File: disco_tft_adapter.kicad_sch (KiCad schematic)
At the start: 0 parts

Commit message: [schematics] addded connectors and adapter wiring
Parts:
- added J1: F31L-1A7H1-11030, aa_prj:F31L1A7H111030, symbol aa_prj:F31L-1A7H1-11030
- added J2: QTH-030-02-L-D-A, aa_prj:QTH-030-XX-Y-D-A, symbol aa_prj:QTH-030-02-L-D-A
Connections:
- new net CTP_INT: J1.25, J2.4
- new net CTP_SCL: J1.27, J2.44
- new net CTP_SDA: J1.26, J2.40
- new net DSI_CLK_N: J1.17, J2.5
- new net DSI_CLK_P: J1.16, J2.3
- new net DSI_D0_N: J1.11, J2.11
- new net DSI_D0_P: J1.10, J2.9
- new net DSI_D1_N: J1.14, J2.17
- new net DSI_D1_P: J1.13, J2.15
- new net GND: J1.12, J1.15, J1.18, J1.21, J1.24, J1.31 (MP_1), J1.32 (MP_2), J1.9, J2.1, J2.13, J2.19, J2.27, J2.29, J2.7
- new net LEDA: J1.1
- new net LEDK: J1.2, J1.3
- new net PWM: J1.8
- new net PWM_UC: J2.53
- new net RST: J1.28, J1.6, J2.57
- new net TE: J1.7, J2.49
- new net VCC: J1.29, J1.30, J1.4, J1.5, J2.36
- new net VCC_BL: J2.21, J2.23
- no-connect marks 0 -> 43
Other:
- note added: "Vcc = 3V3"
- note added: "Vcc_BL = 5V"

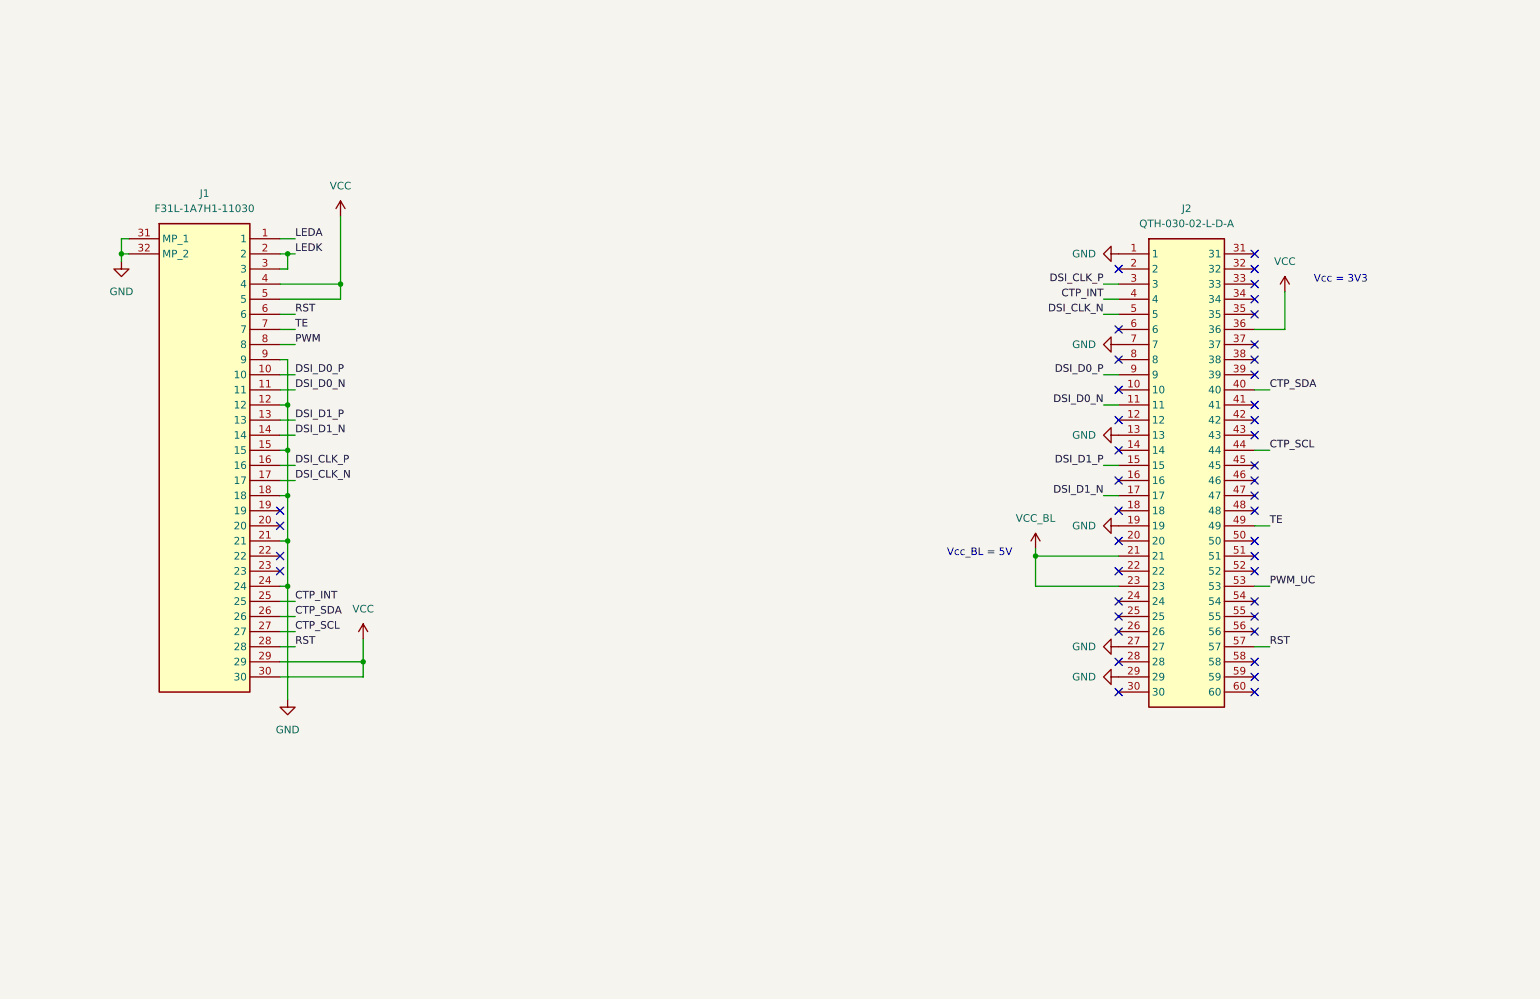
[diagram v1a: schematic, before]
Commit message: [schematics] add: buck converter for backlight control
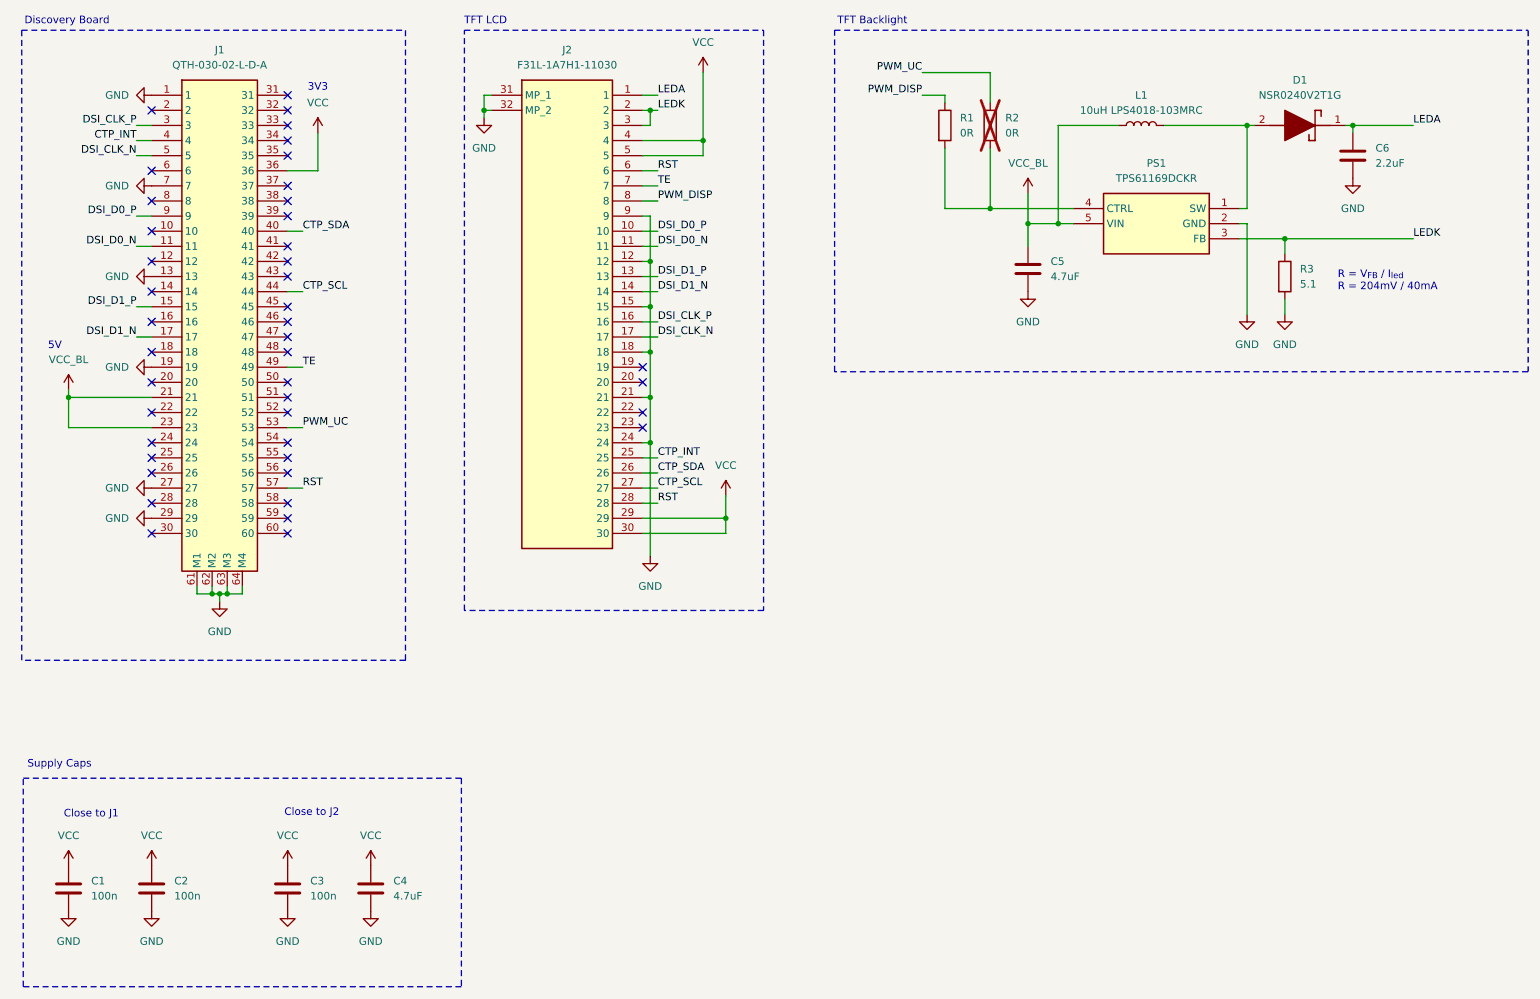
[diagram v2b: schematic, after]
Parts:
- added C1, C2, C3: 100n, Capacitor_SMD:C_0201_0603Metric_Pad0.64x0.40mm_HandSolder, symbol Device:C
- added C4, C5: 4.7uF, Capacitor_SMD:C_0805_2012Metric_Pad1.18x1.45mm_HandSolder, symbol Device:C
- added C6: 2.2uF, Capacitor_SMD:C_0805_2012Metric_Pad1.18x1.45mm_HandSolder, symbol Device:C
- added D1: NSR0240V2T1G, aa_prj:SODFL1608X70N, symbol aa_prj:NSR0240V2T1G
- added L1: 10uH LPS4018-103MRC, Inductor_SMD:L_Coilcraft_1515SQ-47N, symbol Device:L
- added PS1: TPS61169DCKR, aa_prj:SOT65P210X110-5N, symbol aa_prj:TPS61169DCKR
- added R1, R2: 0R, Resistor_SMD:R_0201_0603Metric_Pad0.64x0.40mm_HandSolder, symbol Device:R
- added R3: 5.1, Resistor_SMD:R_1206_3216Metric, symbol Device:R
- renumbered J2 to J1, J1 to J2
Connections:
- net GND: now also J1.61 (M1), J1.62 (M2), J1.63 (M3), J1.64 (M4), C1.2, C2.2, C3.2, C4.2, C5.2, C6.2, PS1.2 (GND), R3.2
- net LEDA: now also C6.1, D1.1 (K)
- net LEDK: now also PS1.3 (FB), R3.1
- net PWM_UC: now also R2.1
- net VCC: now also C1.1, C2.1, C3.1, C4.1
- net VCC_BL: now also C5.1, L1.1, PS1.5 (VIN)
- net PWM renamed PWM_DISP
- net PWM_DISP: now also R1.1
- new net: D1.2 (A), L1.2, PS1.1 (SW)
- new net: PS1.4 (CTRL), R1.2, R2.2
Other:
- note added: "3V3"
- note added: "5V"
- note added: "Close to J1"
- note added: "Close to J2"
- note added: "Discovery Board"
- note added: "R = V_{FB} / I_{led} R = 204mV / 40mA"
- note added: "Supply Caps"
- note added: "TFT Backlight"
- note added: "TFT LCD"
- note removed: "Vcc = 3V3"
- note removed: "Vcc_BL = 5V"
- moved on the sheet: J2

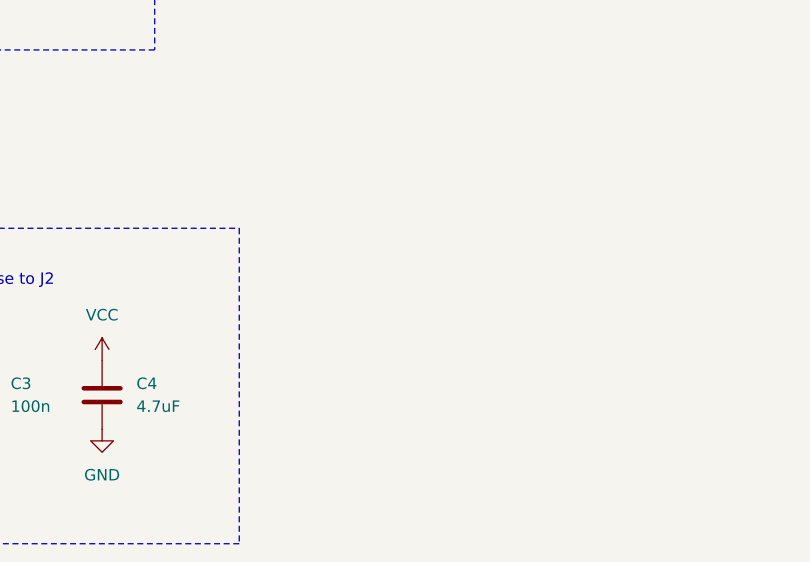
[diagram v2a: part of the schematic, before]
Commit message: [schematics] add: mounting holes
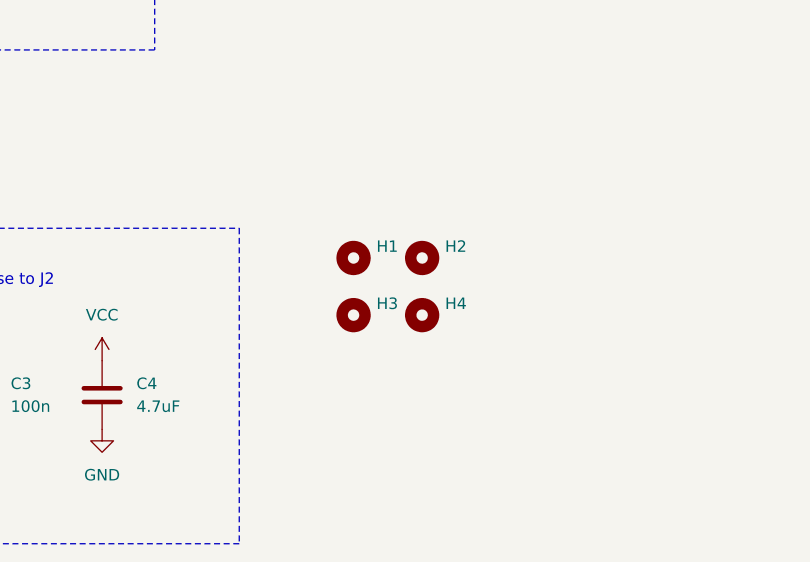
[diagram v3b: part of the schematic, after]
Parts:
- added H1, H2, H3, H4: MountingHole, MountingHole:MountingHole_4.5mm_Pad_TopBottom, symbol Mechanical:MountingHole

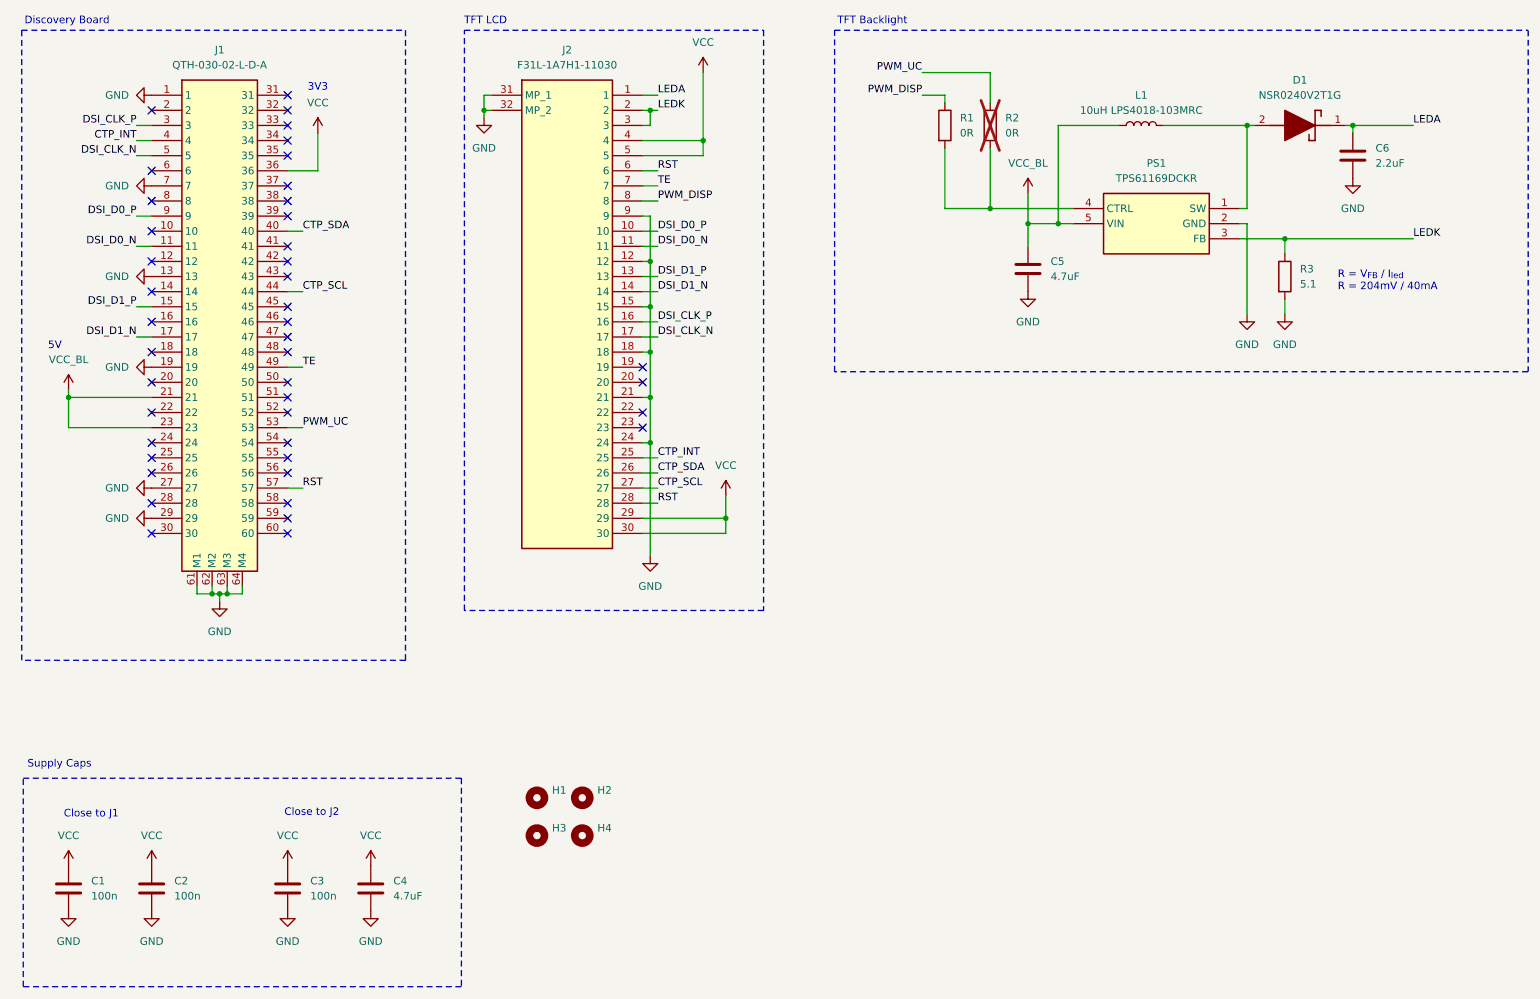
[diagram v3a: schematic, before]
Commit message: [layout] add: stitching vias, planes updated, routed buck converter for LED BL, added power labels to buck converter in schematics
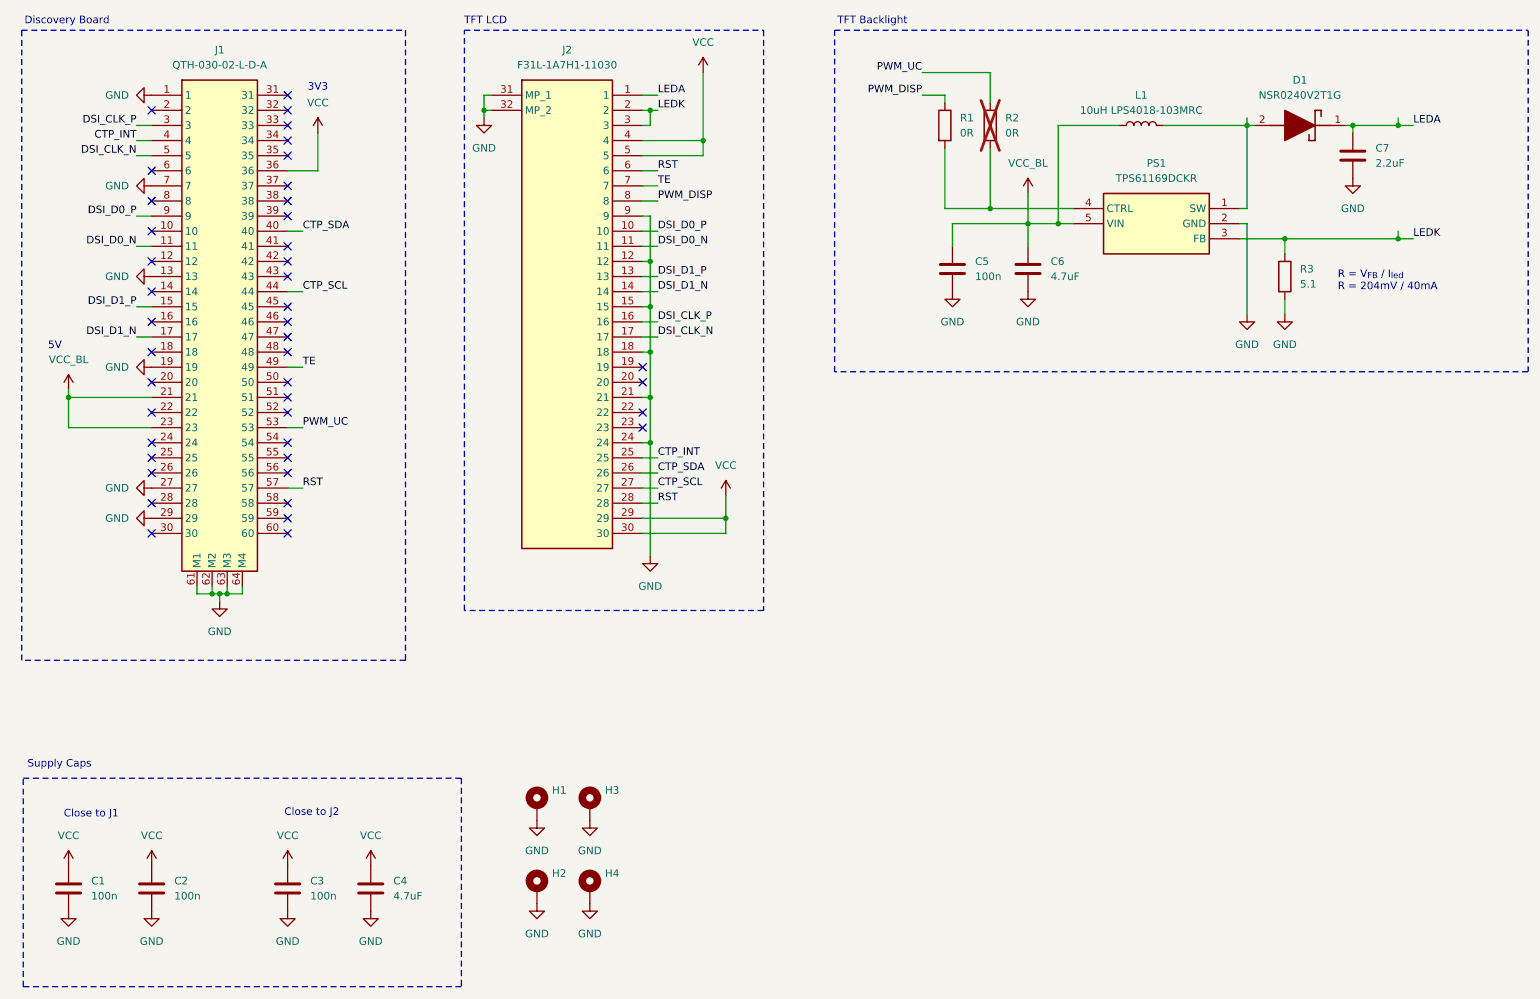
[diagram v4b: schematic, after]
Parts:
- removed H1, H2, H3, H4: MountingHole, MountingHole:MountingHole_4.5mm_Pad_TopBottom, symbol Mechanical:MountingHole
- added C5: 100n, Capacitor_SMD:C_0201_0603Metric_Pad0.64x0.40mm_HandSolder, symbol Device:C
- added H1, H2, H3, H4: MountingHole_Pad, MountingHole:MountingHole_4.5mm_Pad_TopBottom, symbol Mechanical:MountingHole_Pad
- renumbered C5 to C6, C6 to C7
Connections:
- net GND: now also C5.2, H1.1, H2.1, H3.1, H4.1
- net VCC_BL: now also C5.1

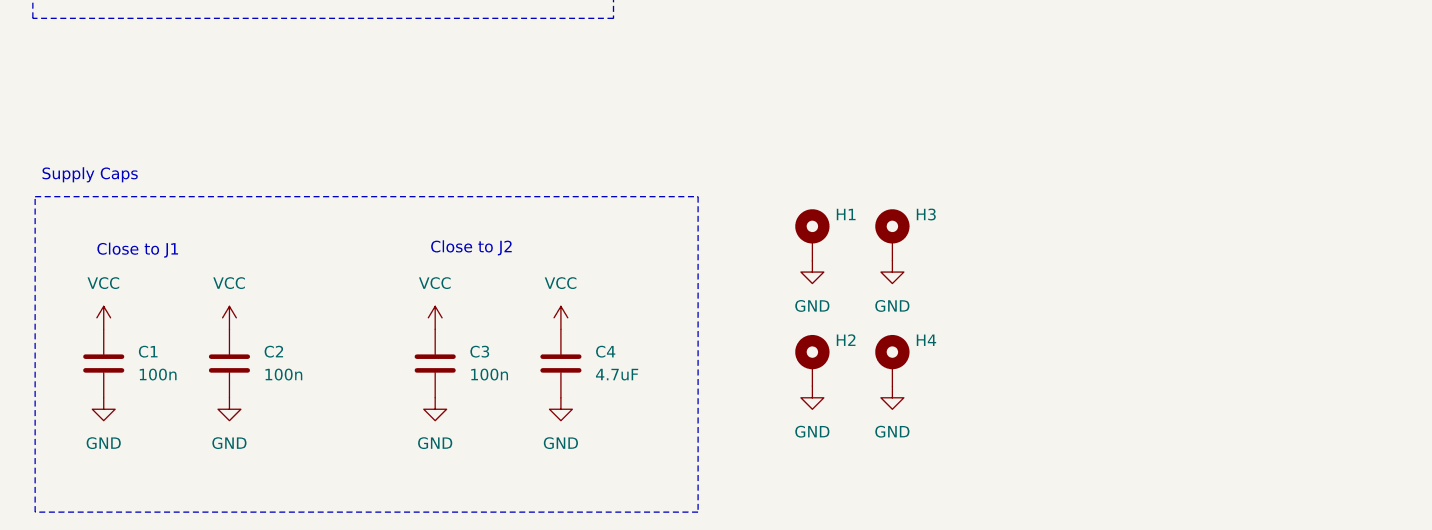
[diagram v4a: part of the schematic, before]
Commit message: [schematics] add: more decoupling C
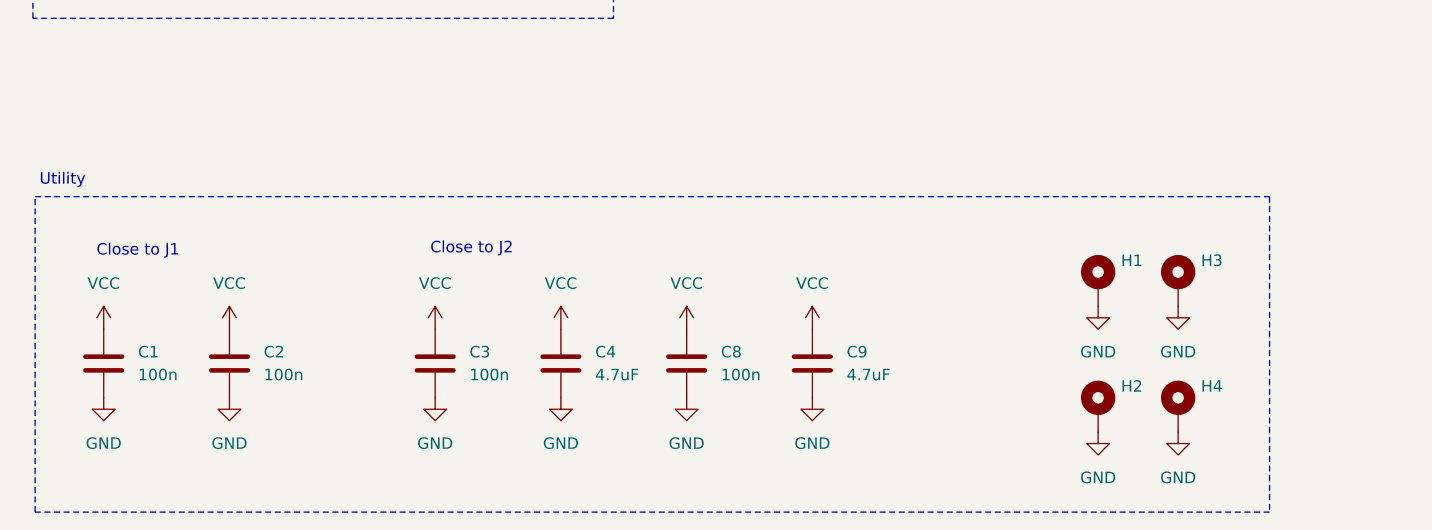
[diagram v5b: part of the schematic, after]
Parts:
- added C8: 100n, Capacitor_SMD:C_0201_0603Metric_Pad0.64x0.40mm_HandSolder, symbol Device:C
- added C9: 4.7uF, Capacitor_SMD:C_0805_2012Metric_Pad1.18x1.45mm_HandSolder, symbol Device:C
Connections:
- net GND: now also C8.2, C9.2
- net VCC: now also C8.1, C9.1
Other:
- note added: "Utility"
- note removed: "Supply Caps"
- moved on the sheet: H1, H2, H3, H4
